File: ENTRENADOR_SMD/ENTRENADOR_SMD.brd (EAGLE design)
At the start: 100 x 100.3 mm, 76 parts, among them IC1 PIC16F1939PT, SW1 TL3342F160QG/TR

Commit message: Se actualiza y se argegan librerias
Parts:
- removed S2: SLDS2, JS202011SCQN:SW_JS202011SCQN
- added IC2: 7824T, linear:TO220H
- added J1: DCJ0202, con-jack:DCJ0202
- added PWR_SLIDE: SLDS2, JS202011SCQN:SW_JS202011SCQN
- added U$1, U$2, U$4, U$5: CAPA, CAPAE830X1000N:CAPA
- added U$3: VREG3V3, VREG_L7805ACD2T:VREG3V3
- added X1: (no value), con-ptr500:AK300/2
- moved PICKIT 8.50 mm to (4.20, 17.4)
- moved USB 7.75 mm to (4.70, 37.2)
- renumbered JP1 to POT, JP2 to JP_5V5, JP3 to JP_3V3, JP4 to SOC_UART, JP5 to JP_I2C, LEDS3 to BTN_A, LEDS4 to BTN_B
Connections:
- removed net GNG: PD.9
- new net N$36: IC2.1, J1.1, U$4.P, X1.1
- net 3V3: now also U$2.P, U$3.4
- net GND: now also IC2.2, J1.2, J1.3, PD.9, U$1.N, U$2.N, U$3.1, U$4.N, U$5.N, X1.2
- net VCC: now also PWR_SLIDE.2, PWR_SLIDE.5, U$1.P, U$3.3; no longer S2.2, S2.5
- net VEXT: now also IC2.3, PWR_SLIDE.3, PWR_SLIDE.6, U$5.P; no longer S2.3, S2.6
- net VUSB: now also PWR_SLIDE.1, PWR_SLIDE.4; no longer S2.1, S2.4
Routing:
- net GND: track 427.3 -> 564.2 mm, vias 3 -> 4
- net VEXT: track 5.50 -> 96.8 mm, vias 0 -> 2
- net 3V3: track 22.9 -> 87.4 mm, vias 0 -> 2
- net N$36: track 0.00 -> 51.3 mm
- net VCC: track 569.8 -> 619.2 mm, vias 5 -> 10
- net VUSB: track 10.7 -> 27.9 mm
- net RB6: track 66.0 -> 75.8 mm, vias 0 -> 2
- net RD3: track 30.2 -> 36.7 mm
- net RB7: track 79.6 -> 86.0 mm, vias 1 -> 3
- net RC5: track 30.2 -> 35.2 mm
- net RC3: track 68.7 -> 73.2 mm
- net MCLR: track 76.7 -> 80.2 mm
- net RC4: track 62.7 -> 63.7 mm
- net RC7: track 49.4 -> 48.6 mm
- net RC1: track 33.1 -> 32.3 mm
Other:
- board size 100 x 100.3 mm -> 99.8 x 100.2 mm
- board text added: "<"

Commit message: se crea diseño entrenador
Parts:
- removed JP_SLIDES1, JP_SLIDES2: (no value), pinhead:1X04
- removed LED1, LED4, LED5, LED8: (no value), led:CHIP-LED0805
- added JP_SLIDES_DOWN, JP_SLIDES_UP: (no value), pinhead:1X04
- added L1, L4, L5, L8: (no value), led:CHIP-LED0805
- added R23, R24, R25, R26, R27, R28, R29, R30: 4K7, R0805_:R0805
- R1: value (none) -> 4K7
- R10, R11, R12, R13, R14, R15, R16, R17: value (none) -> 10K
- R19, R20, R21: value 3386P-1-101TLF -> COM-09806; device 3386P-1-101TLF:TRIM_3386P-1-101TLF -> COM-09806:TRIM_COM-09806
- R2, R3, R4, R5, R6, R7, R8, R9: value (none) -> 330R
- moved R2 90.9 mm to (45.5, 88.8), turned to 270 degrees
- moved R3 90.2 mm to (49.5, 88.8), turned to 270 degrees
- moved R4 89.4 mm to (53.8, 88.8), turned to 270 degrees
- moved R6 89.4 mm to (61.5, 88.8), turned to 270 degrees
- moved R5 88.9 mm to (57.5, 88.8), turned to 270 degrees
- moved R7 88.7 mm to (65.5, 88.8), turned to 270 degrees
- moved R8 88.2 mm to (69.5, 88.8), turned to 270 degrees
- moved R9 87.7 mm to (73.3, 88.8), turned to 270 degrees
- moved PD 79.4 mm to (84.9, 5.15), turned to 0 degrees
- moved LED2 78.5 mm to (53.0, 82.0), turned to 0 degrees
- moved LED3 78.2 mm to (55.9, 82.0), turned to 0 degrees
- moved LED6 78.0 mm to (66.1, 82.0), turned to 0 degrees
- moved LED7 77.7 mm to (69.0, 82.0), turned to 0 degrees
- moved LEDS1 76.5 mm to (80.0, 89.5)
- moved LEDS2 72.6 mm to (80.0, 84.8)
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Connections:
- new net N$37: JP_SLIDES_UP.1, R27.1
- new net N$38: JP_SLIDES_UP.2, R28.1
- new net N$39: JP_SLIDES_UP.3, R29.1
- new net N$40: JP_SLIDES_DOWN.1, R26.1
- new net N$41: JP_SLIDES_DOWN.2, R25.1
- new net N$42: JP_SLIDES_DOWN.3, R24.1
- new net N$43: JP_SLIDES_DOWN.4, R23.1
- new net N$44: JP_SLIDES_UP.4, R30.1
- net N$1: now also R23.2; no longer JP_SLIDES1.4
- net N$12: now also L4.C; no longer LED4.C
- net N$13: now also L5.C; no longer LED5.C
- net N$16: now also L8.C; no longer LED8.C
- net N$17: now also L1.A; no longer LED1.A
- net N$2: now also R24.2; no longer JP_SLIDES1.3
- net N$20: now also L4.A; no longer LED4.A
- net N$21: now also L5.A; no longer LED5.A
- net N$24: now also L8.A; no longer LED8.A
- net N$3: now also R25.2; no longer JP_SLIDES1.2
- net N$4: now also R26.2; no longer JP_SLIDES1.1
- net N$5: now also R30.2; no longer JP_SLIDES2.4
- net N$6: now also R29.2; no longer JP_SLIDES2.3
- net N$7: now also R28.2; no longer JP_SLIDES2.2
- net N$8: now also R27.2; no longer JP_SLIDES2.1
- net N$9: now also L1.C; no longer LED1.C
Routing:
- net GND: track 564.2 -> 420.4 mm, vias 4 -> 11
- net RC7: track 48.6 -> 146.4 mm, vias 1 -> 4
- net RD6: track 36.7 -> 119.7 mm, vias 0 -> 1
- net RD7: track 40.4 -> 122.9 mm, vias 0 -> 1
- net RD5: track 29.1 -> 110.7 mm, vias 0 -> 1
- net RD4: track 28.8 -> 106.7 mm, vias 0 -> 1
- net RC6: track 48.5 -> 119.4 mm, vias 1 -> 3
- net RC4: track 63.7 -> 132.0 mm, vias 1 -> 4
- net RD2: track 26.8 -> 84.4 mm, vias 0 -> 1
- net RD1: track 25.5 -> 78.1 mm, vias 0 -> 1
- net RD0: track 27.1 -> 77.5 mm, vias 0 -> 1
- net RD3: track 36.7 -> 86.8 mm, vias 0 -> 1
- net N$19: track 4.25 -> 50.9 mm, vias 1 -> 0
- net N$30: track 16.3 -> 56.3 mm, vias 1 -> 2
- net RC3: track 73.2 -> 112.4 mm, vias 3 -> 2
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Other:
- board text added: "COMMON"
- board text added: "VEXTERNAL"
- board text added: "VUSB"
- board text removed: "SCL"
- board text removed: "SDA"

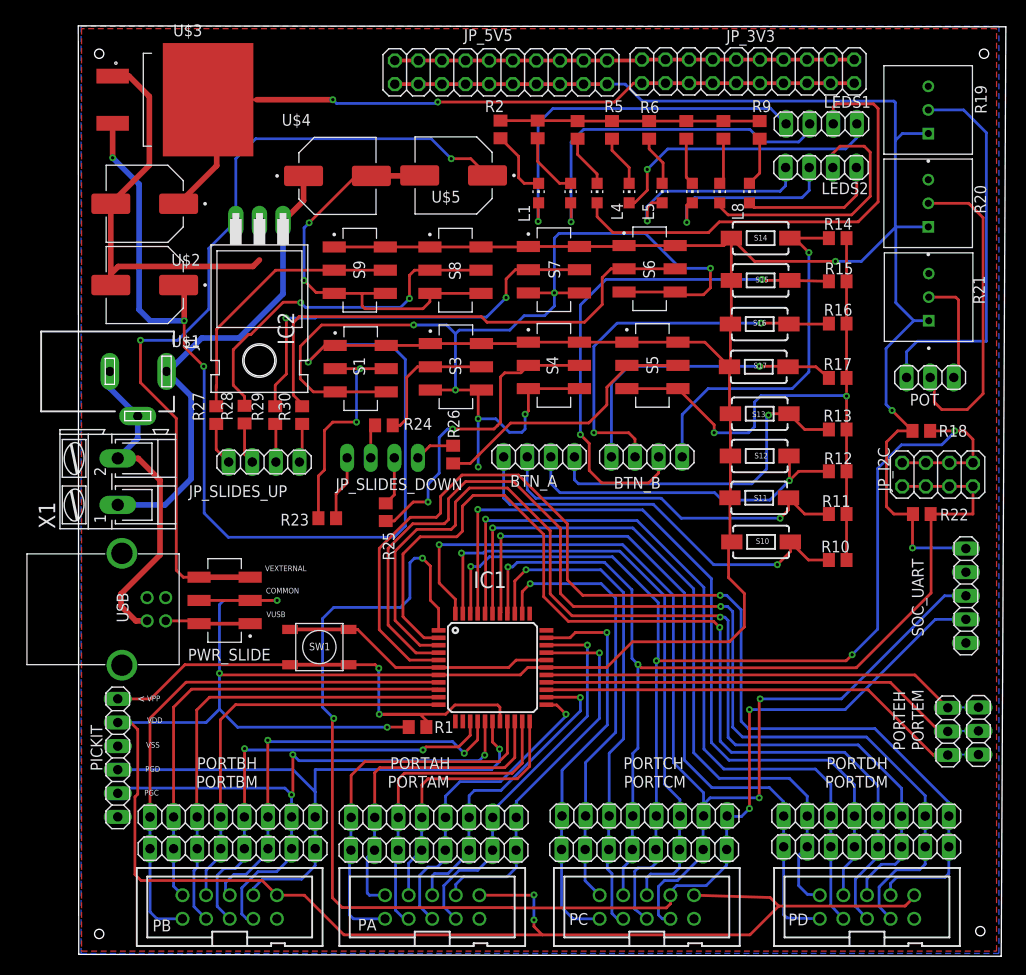
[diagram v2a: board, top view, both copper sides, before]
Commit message: Se ajusta el PCB SMD en perforacion
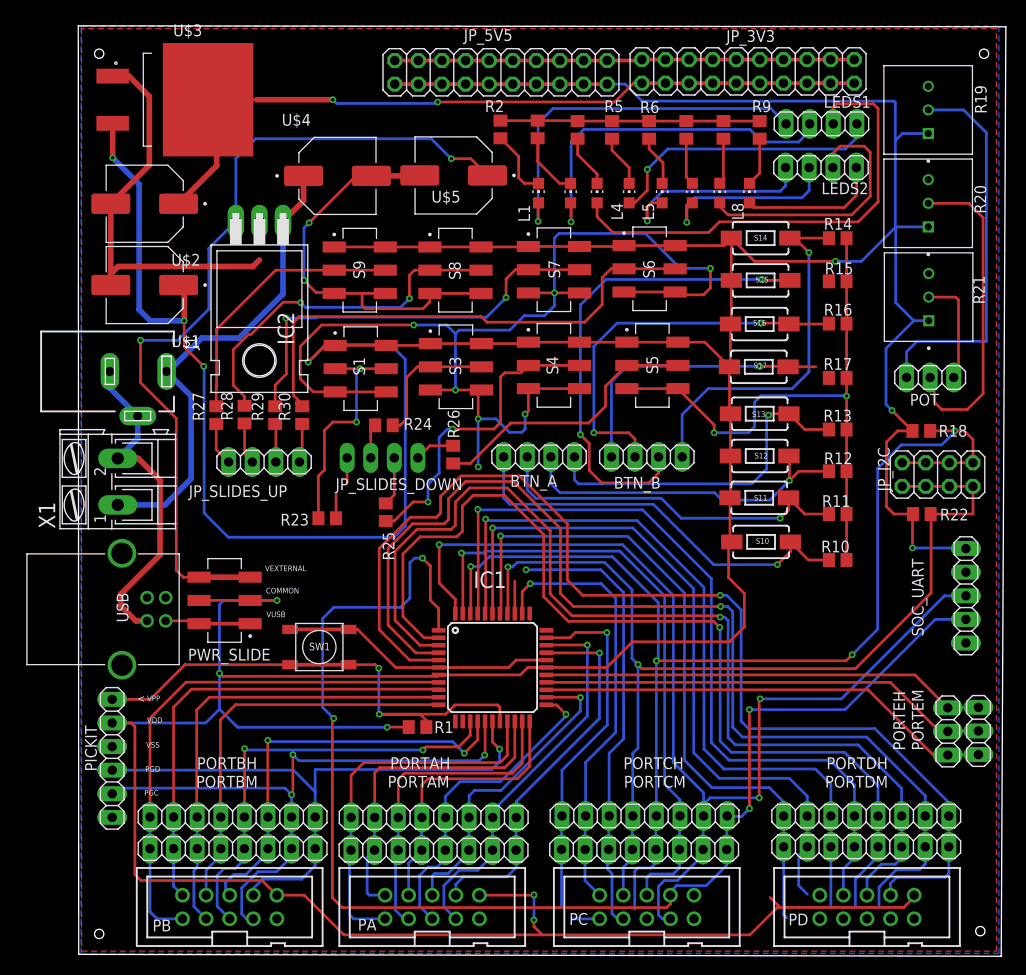
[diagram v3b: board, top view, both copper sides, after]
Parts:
- moved PICKIT 0.60 mm to (3.65, 21.1)
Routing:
- net VCC: track 628.6 -> 621.7 mm
- net N$30: track 56.3 -> 52.1 mm
- net RD0: track 77.5 -> 74.0 mm
- net RD2: track 84.4 -> 82.4 mm
- net RD4: track 106.7 -> 104.9 mm
- net RD6: track 119.7 -> 117.9 mm
- net N$32: track 32.6 -> 30.9 mm
- net RC0: track 43.0 -> 41.3 mm
- net RC2: track 53.7 -> 52.0 mm
- net N$43: track 6.99 -> 5.31 mm
- net RC4: track 132.0 -> 130.3 mm
- net RD1: track 78.1 -> 76.7 mm
- net RB6: track 66.2 -> 66.8 mm
- net MCLR: track 55.8 -> 56.5 mm
- net RB7: track 65.8 -> 66.4 mm
